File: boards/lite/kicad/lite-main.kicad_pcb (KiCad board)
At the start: 2 copper layers, 100 x 90 mm, 134 parts, among them J1 USB4105-GF-A-120, J2 RCA line in, J3 RCA sub out, J4 DB128V-5.08-4P, Q1 AO4485, Q2 MMBT3904, Q3 MMBT3904, Q4 MMBT3904, SW1 TS-1187A, SW2 TS-1187A, SW3 TS-1187A, U1 CH224A, U2 TPS54302, U3 SY8089A1AAC, U4 LP5907-3.3, U5 ESP32-WROVER-E-N8R8, U6 CH340C, U7 ES8388, U8 TPA3118D2, U9 IRM-H638T

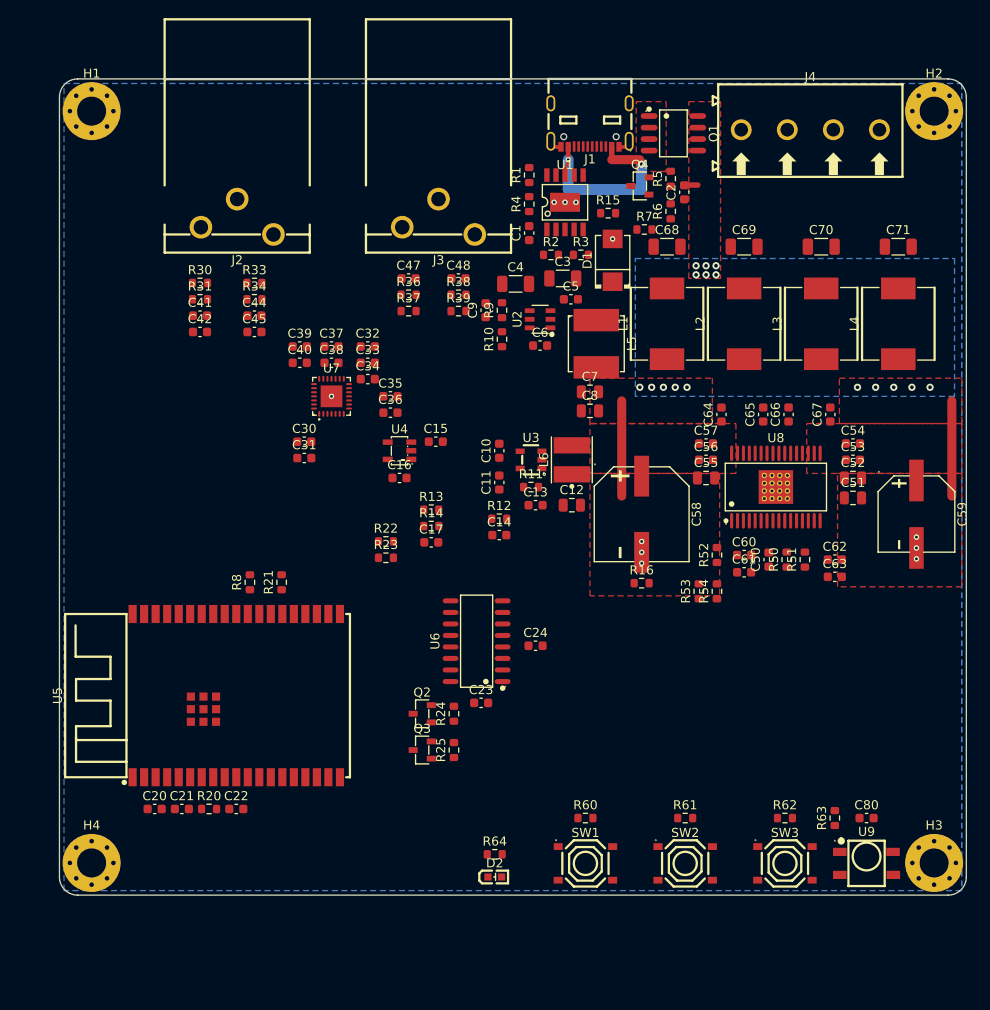
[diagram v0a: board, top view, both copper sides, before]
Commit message: lite-main: routed, drc_routed 0/0; front-facing IR receiver, PVDD sense on GPIO39
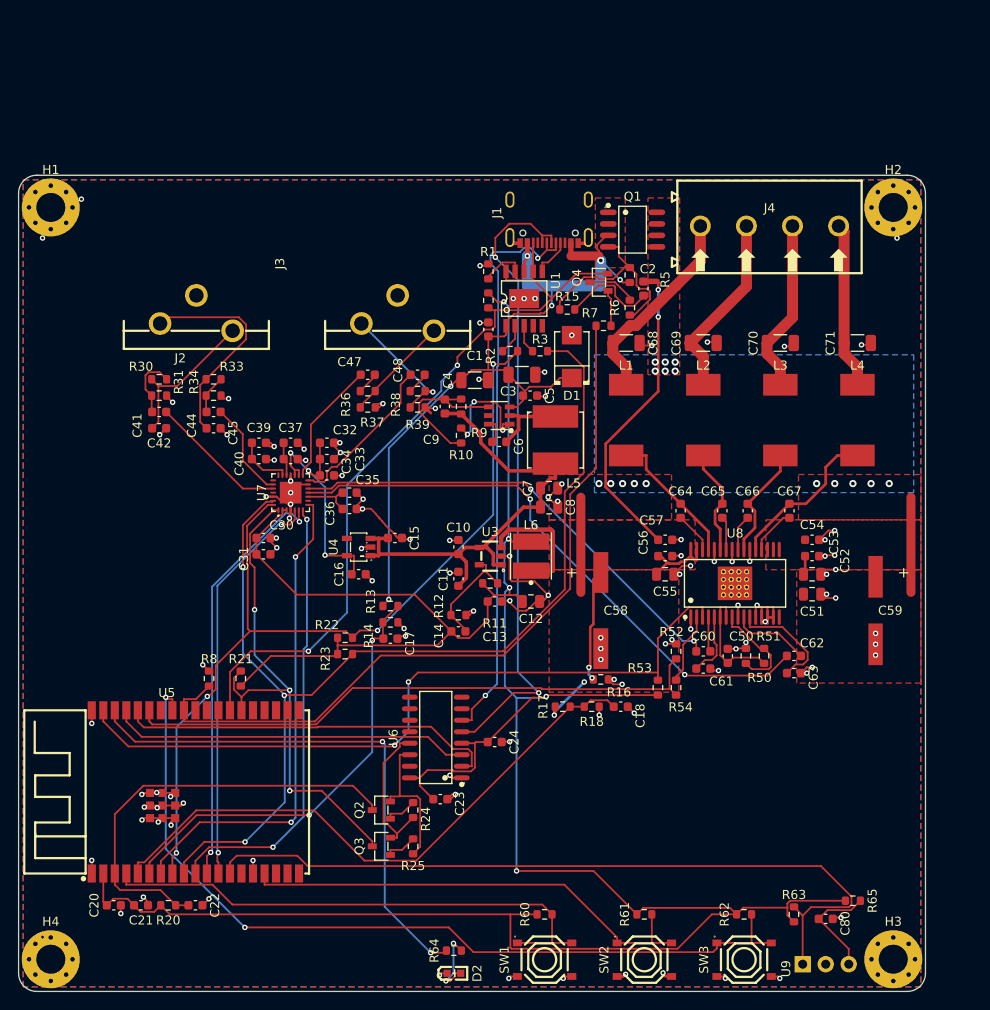
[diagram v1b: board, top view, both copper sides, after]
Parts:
- added C18: 100nF, Capacitor_SMD:C_0603_1608Metric, F.Cu at (89.3, 118.9)
- added R17: 100k, Resistor_SMD:R_0603_1608Metric, F.Cu at (82.9, 118.9)
- added R18: 10k, Resistor_SMD:R_0603_1608Metric, F.Cu at (86.1, 118.9)
- added R65: 100R, Resistor_SMD:R_0603_1608Metric, F.Cu at (114.9, 140.3)
- C80: value 100nF -> 4.7uF
- U9: value IRM-H638T -> IRM-3638T; footprint aiee:SENSOR-SMD_IRM-H638T-TR2-TL -> aiee:OPTO-TH_IRM-3638T
- moved C80 12.0 mm to (111.9, 142.3)
- moved U9 12.0 mm to (111.9, 147.3)
- moved H1 11.5 mm to (26.4, 63.9)
- moved H2 11.5 mm to (119.3, 63.9)
- moved H4 11.5 mm to (26.4, 146.8)
- moved H3 11.5 mm to (119.3, 146.8)
- moved C14 11.5 mm to (71.4, 110.6)
- moved R15 11.5 mm to (83.4, 75.1)
- moved R24 11.5 mm to (66.4, 130.3)
- moved R25 11.5 mm to (66.4, 134.3)
- moved R38 11.5 mm to (66.9, 84.1)
- moved Q2 11.5 mm to (62.9, 130.3)
- moved Q3 11.5 mm to (62.9, 134.3)
- moved R14 11.5 mm to (63.9, 109.6)
- moved R36 11.5 mm to (61.4, 84.1)
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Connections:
- C80 pad 1: +3V3 -> /IR_VCC
- U5 pad 5: unconnected-(U5-SENSOR_VN-Pad5) -> /PVDD_SENSE
- U9 pad 1: GND -> /IR_IN
- U9 pad 3: /IR_IN -> /IR_VCC
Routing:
- net +3V3: track 0.00 -> 307.1 mm, vias 0 -> 5
- net GND: track 1.80 -> 168.0 mm, vias 11 -> 119
- net /I2C_SDA: track 0.00 -> 117.9 mm, vias 0 -> 3
- net /I2C_SCL: track 0.00 -> 98.6 mm, vias 0 -> 4
- net /BTN_PLAY: track 0.00 -> 94.2 mm, vias 0 -> 2
- net /IR_IN: track 0.00 -> 85.4 mm
- net /PVDD_EN: track 0.00 -> 84.7 mm
- net /PD_PG: track 0.00 -> 82.2 mm, vias 0 -> 2
- net /AMP_FAULTZ: track 0.00 -> 82.1 mm, vias 0 -> 2
- net /USB_DP: track 0.00 -> 71.4 mm, vias 0 -> 2
- net VBUS: track 20.8 -> 90.6 mm, vias 2 -> 6
- net /PVDD_SENSE: track 0.00 -> 66.0 mm
- net /AMP_SDZ_IO: track 0.00 -> 65.1 mm
- net /USB_DM: track 0.00 -> 64.1 mm, vias 0 -> 2
- net /AMP_IN_R: track 0.00 -> 64.1 mm, vias 0 -> 2
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- added copper zone on F.Cu, net GND
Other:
- board text added: "+"

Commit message: lite-main: PVDD drain column on B.Cu, R16 out of the pour; re-routed, drc_routed 0/0
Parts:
- moved R16 6.38 mm to (82.9, 120.7)
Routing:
- net PVDD: track 85.0 -> 50.8 mm, vias 22 -> 18
- net GND: track 168.0 -> 149.5 mm, vias 119 -> 109
- net /VBUS_SENSE: track 48.7 -> 65.0 mm
- net /I2C_SCL: track 98.6 -> 109.9 mm, vias 4 -> 5
- net /PVDD_EN: track 84.7 -> 74.9 mm, vias 0 -> 2
- net /BUCK3_LX: track 14.0 -> 4.36 mm
- net /LINEIN_R: track 23.9 -> 14.7 mm, vias 0 -> 1
- net /ESP_EN: track 47.9 -> 39.2 mm, vias 0 -> 4
- net /I2C_SDA: track 117.9 -> 110.5 mm, vias 3 -> 4
- net /IR_IN: track 85.4 -> 78.1 mm, vias 0 -> 2
- net /SUB_R: track 14.4 -> 20.9 mm, vias 1 -> 0
- net /USB_DP: track 71.4 -> 65.1 mm
- net +3V3: track 307.1 -> 313.0 mm
- net /I2S_DIN: track 54.1 -> 48.2 mm
- net /AMP_SDZ_IO: track 65.1 -> 70.7 mm
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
